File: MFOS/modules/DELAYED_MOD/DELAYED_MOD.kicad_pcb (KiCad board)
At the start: 2 copper layers, 160 x 100 mm, 16 parts, among them J1 Card Connector, Q1 2N3906, Q3 2N3904, X1 WireConnector, X2 WireConnector, X5 WireConnector, X9 WireConnector

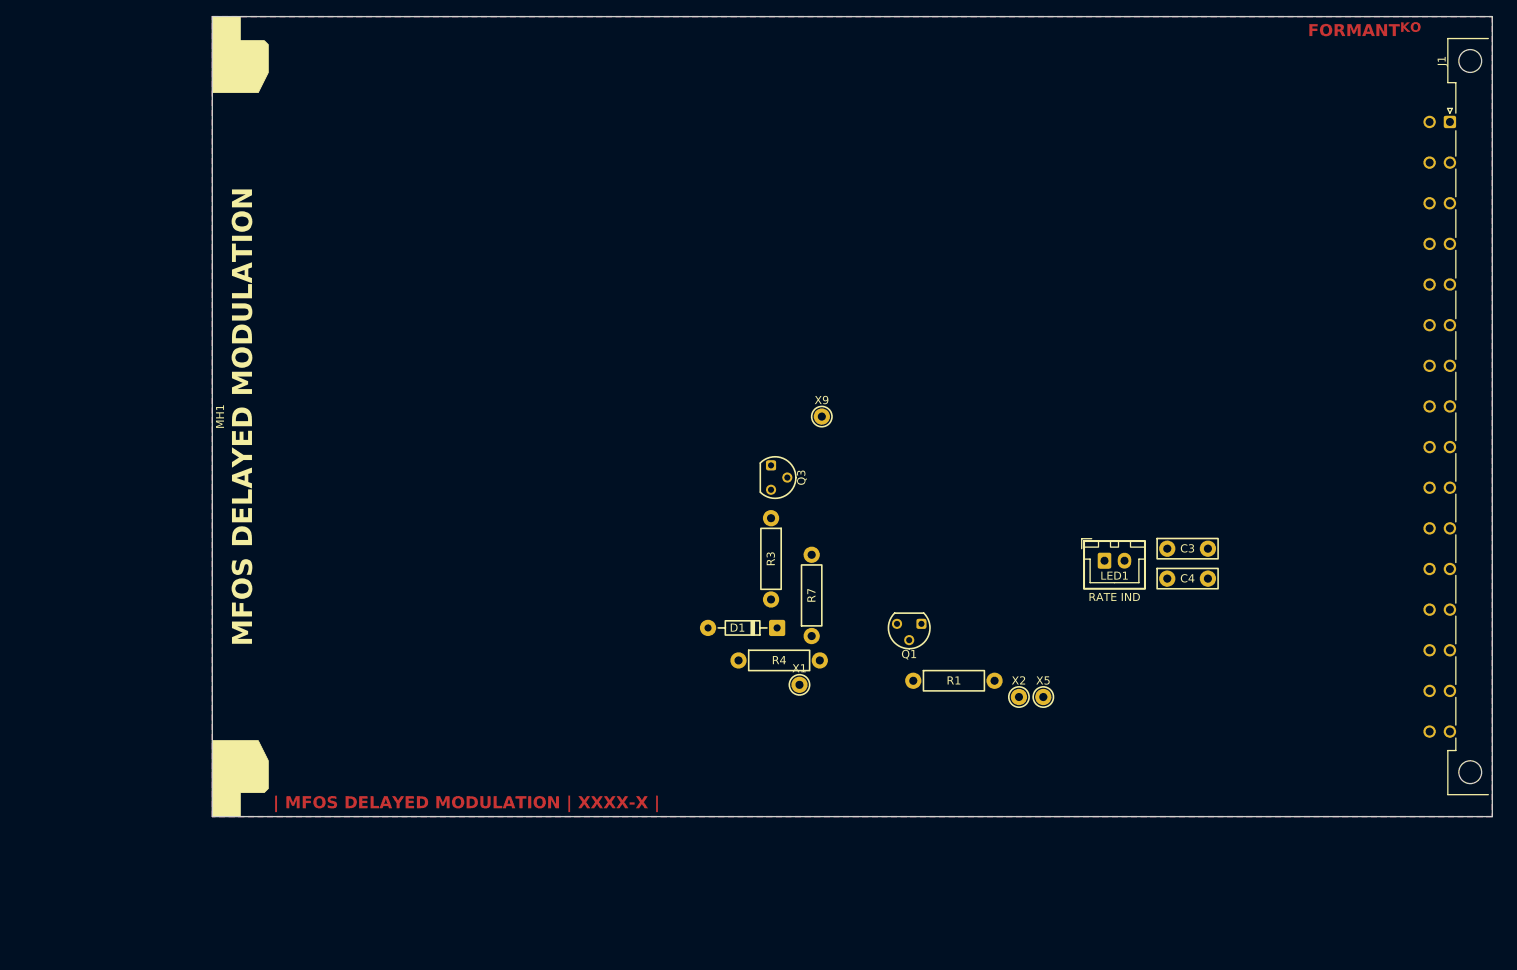
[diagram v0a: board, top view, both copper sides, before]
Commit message: added delayed modulation
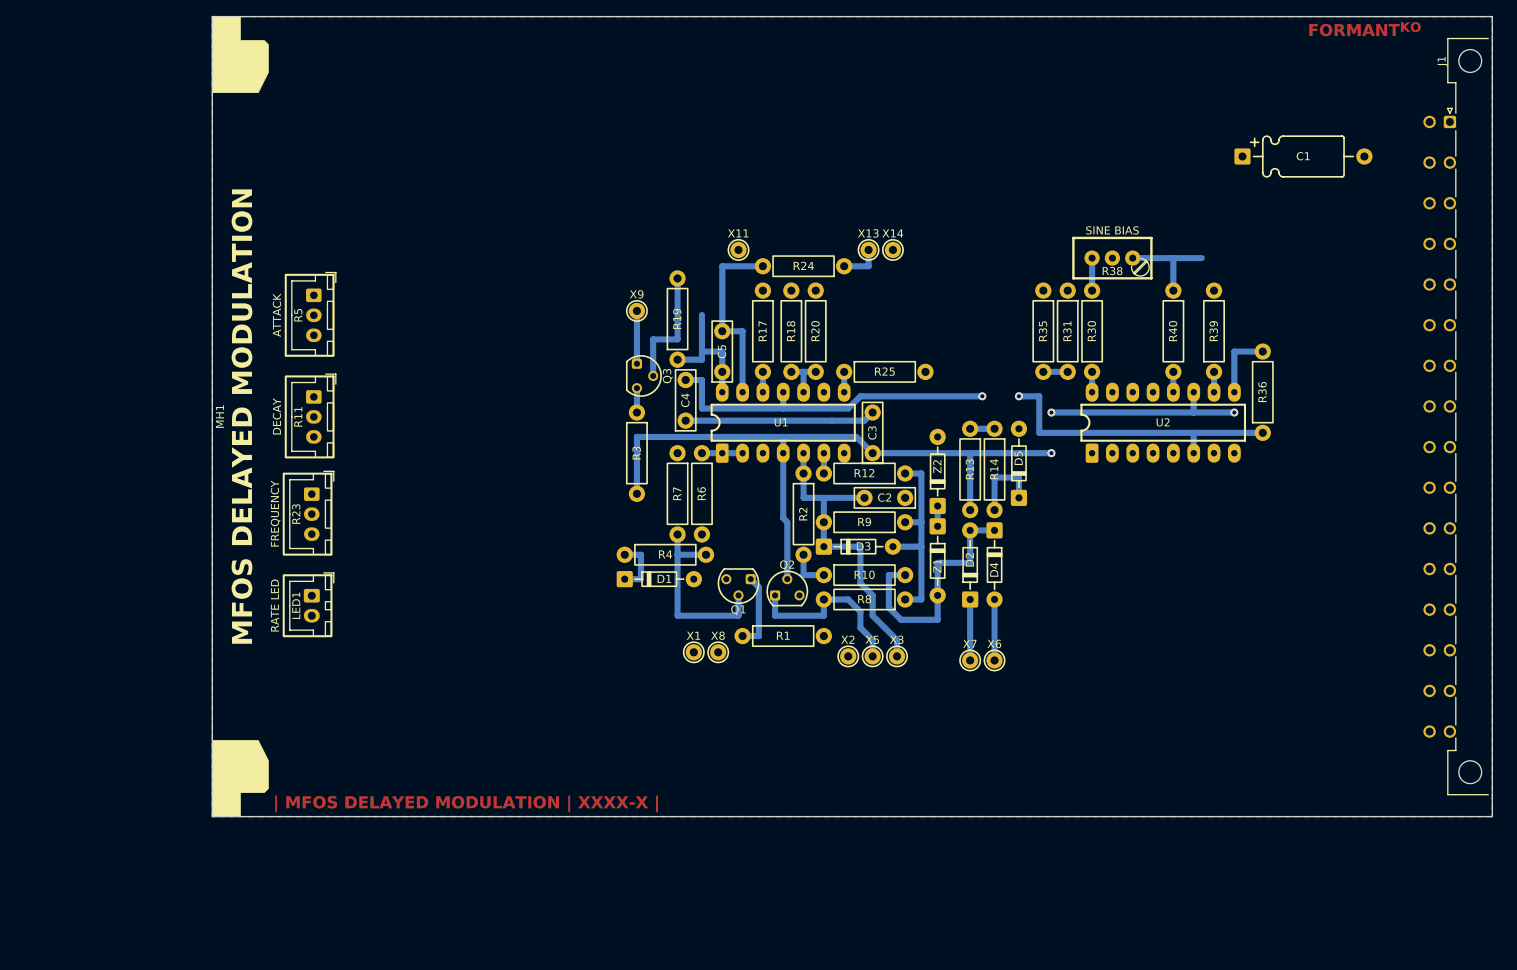
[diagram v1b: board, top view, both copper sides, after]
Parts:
- added C1: 4µ7, FormantKO:CP_Axial_P600mil, F.Cu at (191.4, 62.5)
- added C2: 2n2, FormantKO:C_Rect_P200mil, F.Cu at (139.1, 105.2)
- added C5: 22n, FormantKO:C_Rect_P200mil, F.Cu at (118.7, 86.9)
- added D2: 1N4148, FormantKO:DO-35_P340mil, F.Cu at (149.7, 113.5)
- added D3: 1N4148, FormantKO:DO-35_P340mil, F.Cu at (135.8, 111.3)
- added D4: 1N4148, FormantKO:DO-35_P340mil, F.Cu at (152.8, 113.5)
- added D5: 1N4148, FormantKO:DO-35_P340mil, F.Cu at (155.8, 100.8)
- added Q2: 2N5457, FormantKO:TO-92_MFOS, F.Cu at (126.9, 116.3)
- added R10: 1k, FormantKO:R_Axial_Horizontal_P400mil, F.Cu at (136.5, 114.8)
- added R11: 1M, FormantKO:PanelConnector_1x03, F.Cu at (67.7, 95.0)
- added R12: 47k, FormantKO:R_Axial_Horizontal_P400mil, F.Cu at (136.5, 102.1)
- added R13: 1M, FormantKO:R_Axial_Horizontal_P400mil, F.Cu at (149.7, 101.6)
- added R14: 39k, FormantKO:R_Axial_Horizontal_P400mil, F.Cu at (152.8, 101.6)
- added R17: 220Ω, FormantKO:R_Axial_Horizontal_P400mil, F.Cu at (123.8, 84.3)
- added R18: 47k, FormantKO:R_Axial_Horizontal_P400mil, F.Cu at (127.4, 84.3)
- added R19: 100k, FormantKO:R_Axial_Horizontal_P400mil, F.Cu at (113.2, 82.8)
- added R2: 91k, FormantKO:R_Axial_Horizontal_P400mil, F.Cu at (128.9, 107.2)
- added R20: 100k, FormantKO:R_Axial_Horizontal_P400mil, F.Cu at (130.4, 84.3)
- added R23: 100k, FormantKO:PanelConnector_1x03, F.Cu at (67.4, 107.2)
- added R24: 47k, FormantKO:R_Axial_Horizontal_P400mil, F.Cu at (128.9, 76.2)
- added R25: 5k6, FormantKO:R_Axial_Horizontal_P400mil, F.Cu at (139.1, 89.4)
- added R30: 56k, FormantKO:R_Axial_Horizontal_P400mil, F.Cu at (165.0, 84.3)
- added R31: 100k, FormantKO:R_Axial_Horizontal_P400mil, F.Cu at (161.9, 84.3)
- added R35: 1k8, FormantKO:R_Axial_Horizontal_P400mil, F.Cu at (158.9, 84.3)
- added R36: 4k7, FormantKO:R_Axial_Horizontal_P400mil, F.Cu at (186.3, 92.0)
- added R38: 100k, FormantKO:Potentiometer_Trimmer_MultiTurn, F.Cu at (167.5, 75.2)
- added R39: 15k, FormantKO:R_Axial_Horizontal_P400mil, F.Cu at (180.2, 84.3)
- added R40: 18k, FormantKO:R_Axial_Horizontal_P400mil, F.Cu at (175.1, 84.3)
- added R5: 1M, FormantKO:PanelConnector_1x03, F.Cu at (67.7, 82.3)
- added R6: 3k, FormantKO:R_Axial_Horizontal_P400mil, F.Cu at (116.2, 104.7)
- added R8: 1M, FormantKO:R_Axial_Horizontal_P400mil, F.Cu at (136.5, 117.9)
- added R9: 30k, FormantKO:R_Axial_Horizontal_P400mil, F.Cu at (136.5, 108.2)
- added U1: TL074, FormantKO:DIP-14N, F.Cu at (126.4, 95.8)
- added U2: LM13700, FormantKO:DIP-16N, F.Cu at (173.9, 95.8)
- added X11: WireConnector, FormantKO:Wire_1x01_D40mil_OD80mil, F.Cu at (120.8, 74.2)
- added X13: WireConnector, FormantKO:Wire_1x01_D40mil_OD80mil, F.Cu at (137.0, 74.2)
- added X14: WireConnector, FormantKO:Wire_1x01_D40mil_OD80mil, F.Cu at (140.1, 74.2)
- added X3: WireConnector, FormantKO:Wire_1x01_D40mil_OD80mil, F.Cu at (140.6, 125.0)
- added X6: WireConnector, FormantKO:Wire_1x01_D40mil_OD80mil, F.Cu at (152.8, 125.5)
- added X7: WireConnector, FormantKO:Wire_1x01_D40mil_OD80mil, F.Cu at (149.7, 125.5)
- added X8: WireConnector, FormantKO:Wire_1x01_D40mil_OD80mil, F.Cu at (118.2, 124.5)
- added Z1: type="" model="1N5231" lib="semiconductor.lib", FormantKO:DO-35_P340mil, F.Cu at (145.7, 113.0)
- added Z2: type="" model="1N5231" lib="semiconductor.lib", FormantKO:DO-35_P340mil, F.Cu at (145.7, 101.9)
- Q1, Q3: footprint FormantKO:TO-92 -> FormantKO:TO-92_MFOS
- moved LED1 100.5 mm to (67.4, 118.6), turned to -90 degrees
- moved C4 66.6 mm to (114.2, 93.0), turned to 90 degrees
- moved C3 41.9 mm to (137.5, 97.0), turned to 90 degrees
- moved X9 26.6 mm to (108.1, 81.8)
- moved R1 22.1 mm to (126.4, 122.4)
- moved X2 21.9 mm to (134.5, 125.0)
- moved X5 21.9 mm to (137.5, 125.0)
- moved Q1 21.9 mm to (120.8, 116.3)
- moved R3 21.3 mm to (108.1, 99.6)
- moved R7 21.0 mm to (113.2, 104.7), turned to -90 degrees
- moved Q3 20.6 mm to (109.1, 89.9)
- moved R4 19.4 mm to (111.6, 112.3)
- moved X1 13.8 mm to (115.2, 124.5)
- moved D1 12.1 mm to (110.9, 115.3), turned to 0 degrees
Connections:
- J1 pad a4: unconnected-(J1-GATE1-Pada4) -> GATE1
- J1 pad b4: unconnected-(J1-GATE2-Padb4) -> GATE1
- Q3 pad 2: unconnected-(Q3-B-Pad2) -> Net-(Q3-B)
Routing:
- net +15V: track 0.00 -> 114.3 mm, vias 0 -> 3
- net -15V: track 0.00 -> 80.9 mm, vias 0 -> 2
- net GND: track 0.00 -> 64.4 mm
- net Net-(D3-K): track 0.00 -> 39.5 mm
- net Net-(D2-A): track 0.00 -> 31.1 mm
- net Net-(Q1-B): track 0.00 -> 23.9 mm
- net Net-(U1D--): track 0.00 -> 23.4 mm
- net Net-(Q2-D): track 0.00 -> 22.1 mm
- net TRIANGLE: track 0.00 -> 16.3 mm
- net Net-(Q3-B): track 0.00 -> 15.2 mm
- net Net-(D5-K): track 0.00 -> 9.65 mm
- net Net-(Q1-E): track 0.00 -> 9.56 mm
- net SINE: track 0.00 -> 8.64 mm
- net Net-(D4-A): track 0.00 -> 7.62 mm
- net Net-(D2-K): track 0.00 -> 7.62 mm
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
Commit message: delayed modulation pcb
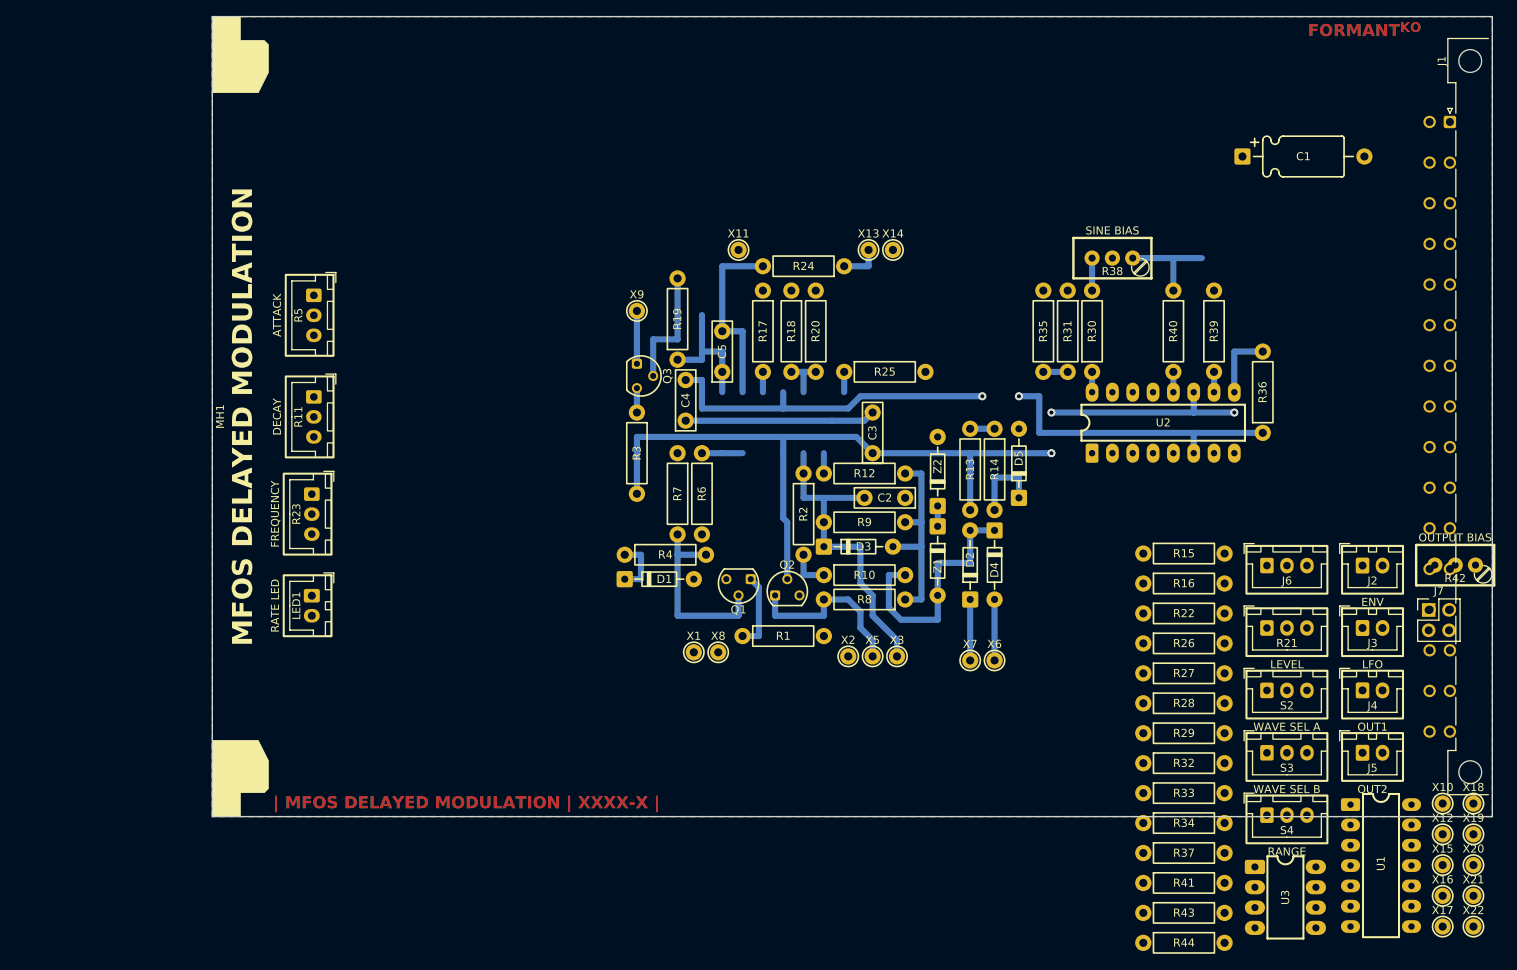
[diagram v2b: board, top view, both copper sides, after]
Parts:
- added J2: MonoJack, FormantKO:PanelConnector_1x02, F.Cu at (200.0, 113.6)
- added J3: MonoJack, FormantKO:PanelConnector_1x02, F.Cu at (200.0, 121.4)
- added J4: MonoJack, FormantKO:PanelConnector_1x02, F.Cu at (200.0, 129.2)
- added J5: MonoJack, FormantKO:PanelConnector_1x02, F.Cu at (200.0, 137.0)
- added J6: GATE, FormantKO:PanelConnector_1x03, F.Cu at (189.3, 113.6)
- added J7: GATE SELECT, Connector_PinHeader_2.54mm:PinHeader_2x02_P2.54mm_Vertical, F.Cu at (207.0, 119.2)
- added R15: 100k, FormantKO:R_Axial_Horizontal_P400mil, F.Cu at (176.5, 112.1)
- added R16: 3k, FormantKO:R_Axial_Horizontal_P400mil, F.Cu at (176.5, 115.9)
- added R21: 100k, FormantKO:PanelConnector_1x03, F.Cu at (189.3, 121.4)
- added R22: 3k, FormantKO:R_Axial_Horizontal_P400mil, F.Cu at (176.5, 119.6)
- added R26: 10k, FormantKO:R_Axial_Horizontal_P400mil, F.Cu at (176.5, 123.3)
- added R27: 4k7, FormantKO:R_Axial_Horizontal_P400mil, F.Cu at (176.5, 127.1)
- added R28: 47k, FormantKO:R_Axial_Horizontal_P400mil, F.Cu at (176.5, 130.8)
- added R29: 7k5, FormantKO:R_Axial_Horizontal_P400mil, F.Cu at (176.5, 134.6)
- added R32: 200K, FormantKO:R_Axial_Horizontal_P400mil, F.Cu at (176.5, 138.3)
- added R33: 1K, FormantKO:R_Axial_Horizontal_P400mil, F.Cu at (176.5, 142.1)
- added R34: 4k7, FormantKO:R_Axial_Horizontal_P400mil, F.Cu at (176.5, 145.8)
- added R37: 3k, FormantKO:R_Axial_Horizontal_P400mil, F.Cu at (176.5, 149.6)
- added R41: 100k, FormantKO:R_Axial_Horizontal_P400mil, F.Cu at (176.5, 153.3)
- added R42: 100k, FormantKO:Potentiometer_Trimmer_MultiTurn, F.Cu at (210.4, 113.6)
- added R43: 200K, FormantKO:R_Axial_Horizontal_P400mil, F.Cu at (176.5, 157.0)
- added R44: 47k, FormantKO:R_Axial_Horizontal_P400mil, F.Cu at (176.5, 160.8)
- added S2: SW, FormantKO:PanelConnector_1x03, F.Cu at (189.3, 129.2)
- added S3: SW, FormantKO:PanelConnector_1x03, F.Cu at (189.3, 137.0)
- added S4: SW, FormantKO:PanelConnector_1x03, F.Cu at (189.3, 144.8)
- added U3: TL072, FormantKO:DIP-8N, F.Cu at (189.1, 155.1)
- added X10: WireConnector, FormantKO:Wire_1x01_D40mil_OD80mil, F.Cu at (208.8, 143.4)
- added X12: WireConnector, FormantKO:Wire_1x01_D40mil_OD80mil, F.Cu at (208.8, 147.2)
- added X15: WireConnector, FormantKO:Wire_1x01_D40mil_OD80mil, F.Cu at (208.8, 151.1)
- added X16: WireConnector, FormantKO:Wire_1x01_D40mil_OD80mil, F.Cu at (208.8, 154.9)
- added X17: WireConnector, FormantKO:Wire_1x01_D40mil_OD80mil, F.Cu at (208.8, 158.7)
- added X18: WireConnector, FormantKO:Wire_1x01_D40mil_OD80mil, F.Cu at (212.6, 143.4)
- added X19: WireConnector, FormantKO:Wire_1x01_D40mil_OD80mil, F.Cu at (212.6, 147.2)
- added X20: WireConnector, FormantKO:Wire_1x01_D40mil_OD80mil, F.Cu at (212.6, 151.1)
- added X21: WireConnector, FormantKO:Wire_1x01_D40mil_OD80mil, F.Cu at (212.6, 154.9)
- added X22: WireConnector, FormantKO:Wire_1x01_D40mil_OD80mil, F.Cu at (212.6, 158.7)
- moved U1 93.0 mm to (201.1, 151.1), turned to 0 degrees
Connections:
- net AR renamed ENV
- net IAR renamed IENV
- J1 pad b4: GATE1 -> GATE2
- U2 pad 1: unconnected-(U2-Pad1) -> Net-(R28-Pad1)
- U2 pad 3: unconnected-(U2C-+-Pad3) -> Net-(U2C-+)
- U2 pad 4: unconnected-(U2C---Pad4) -> GND
- U2 pad 5: unconnected-(U2-Pad5) -> Net-(R43-Pad2)
- U2 pad 7: unconnected-(U2-Pad7) -> Net-(R43-Pad2)
- U2 pad 8: unconnected-(U2-Pad8) -> Net-(R21-Pad3)

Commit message: delayed modulation pcb work
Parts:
- removed J5: MonoJack, FormantKO:PanelConnector_1x02
- removed S3: SW, FormantKO:PanelConnector_1x03
- added C6: 10µ, FormantKO:CP_Radial_P100mil, F.Cu at (197.2, 89.9)
- added C7: 100n, FormantKO:C_Rect_P200mil, F.Cu at (166.8, 105.2)
- added C8: 100n, FormantKO:C_Rect_P200mil, F.Cu at (166.8, 83.6)
- added C9: 10µ, FormantKO:CP_Radial_P100mil, F.Cu at (197.2, 101.1)
- added J10: -15V, FormantKO:Wire_1x01_D40mil_OD80mil, F.Cu at (192.2, 83.3)
- added J8: +15V, FormantKO:Wire_1x01_D40mil_OD80mil, F.Cu at (192.2, 73.4)
- added J9: GND, FormantKO:Wire_1x01_D40mil_OD80mil, F.Cu at (192.2, 78.5)
- C1: footprint FormantKO:CP_Axial_P600mil -> FormantKO:CP_Radial_Tantal_P200mil
- D1, D2, D3, D4, D5: footprint FormantKO:DO-35_P340mil -> FormantKO:DO-35_P400mil
- Q1, Q2, Q3: footprint FormantKO:TO-92_MFOS -> FormantKO:TO-92_Wide
- R1, R10, R12, R13, R14, R15, R16, R17, R18, R19, R2, R20, R22, R24, R25, R26, R27, R28, R29, R3, R30, R31, R32, R33, R34, R35, R36, R37, R4, R6, R7, R8, R9: footprint FormantKO:R_Axial_Horizontal_P400mil -> FormantKO:R_Axial_Horizontal_P500mil
- S2: value SW -> WAVE SELECT; footprint FormantKO:PanelConnector_1x03 -> FormantKO:PanelConnector_1x04
- Z1, Z2: value type="" model="1N5231" lib="semiconductor.lib" -> 1N5231; footprint FormantKO:DO-35_P340mil -> FormantKO:DO-35_P400mil
- moved J3 145.6 mm to (67.7, 60.7), turned to -90 degrees
- moved J4 144.6 mm to (67.7, 70.9), turned to -90 degrees
- moved X15 136.4 mm to (99.4, 69.6)
- moved J2 133.1 mm to (75.3, 67.1), turned to -90 degrees
- moved J6 118.6 mm to (75.3, 81.1), turned to -90 degrees
- moved R21 117.0 mm to (75.3, 95.0), turned to -90 degrees
- moved S2 115.2 mm to (75.3, 112.8), turned to 90 degrees
- moved S4 114.2 mm to (76.6, 126.8), turned to -90 degrees
- moved X16 113.6 mm to (133.7, 69.6)
- moved U1 104.1 mm to (113.4, 95.0), turned to 90 degrees
- moved C1 96.3 mm to (107.1, 109.0), turned to 90 degrees
- moved X17 86.6 mm to (183.3, 76.0)
- moved X20 79.3 mm to (187.1, 76.0)
- moved X19 69.3 mm to (146.4, 126.8)
- moved R27 65.6 mm to (127.4, 83.6)
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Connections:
- R41 pad 2: Net-(S3-c) -> Net-(S2-C)
- S2 pad 1: TRIANGLE -> SQUARE
- S2 pad 2: Net-(S2-c) -> TRIANGLE
- U3 pad 3: Net-(S3-c) -> Net-(S2-C)
- X18 pad 1: Net-(S3-c) -> Net-(S2-C)
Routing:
- net +15V: track 114.3 -> 0.00 mm
- net -15V: track 80.9 -> 0.00 mm
- net GND: track 64.4 -> 0.00 mm
- net Net-(D3-K): track 39.5 -> 0.00 mm
- net Net-(D2-A): track 31.1 -> 0.00 mm
- net Net-(Q1-B): track 23.9 -> 0.00 mm
- net Net-(U1D--): track 23.4 -> 0.00 mm
- net Net-(Q2-D): track 22.1 -> 0.00 mm
- net TRIANGLE: track 16.3 -> 0.00 mm
- net Net-(Q3-B): track 15.2 -> 0.00 mm
- net Net-(D5-K): track 9.65 -> 0.00 mm
- net Net-(Q1-E): track 9.56 -> 0.00 mm
- net SINE: track 8.64 -> 0.00 mm
- net Net-(D4-A): track 7.62 -> 0.00 mm
- net Net-(D2-K): track 7.62 -> 0.00 mm
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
